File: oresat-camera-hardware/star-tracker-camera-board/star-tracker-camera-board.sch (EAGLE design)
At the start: 46 parts, among them J1 3-1734742-6, U1 AR0134CSSM00SPCA0, U2 TPS70618DRVR, U3 TPS71928-28DRVT, U4 TPS71928-28DRVT, X1 KC2520B27.0000C10E00

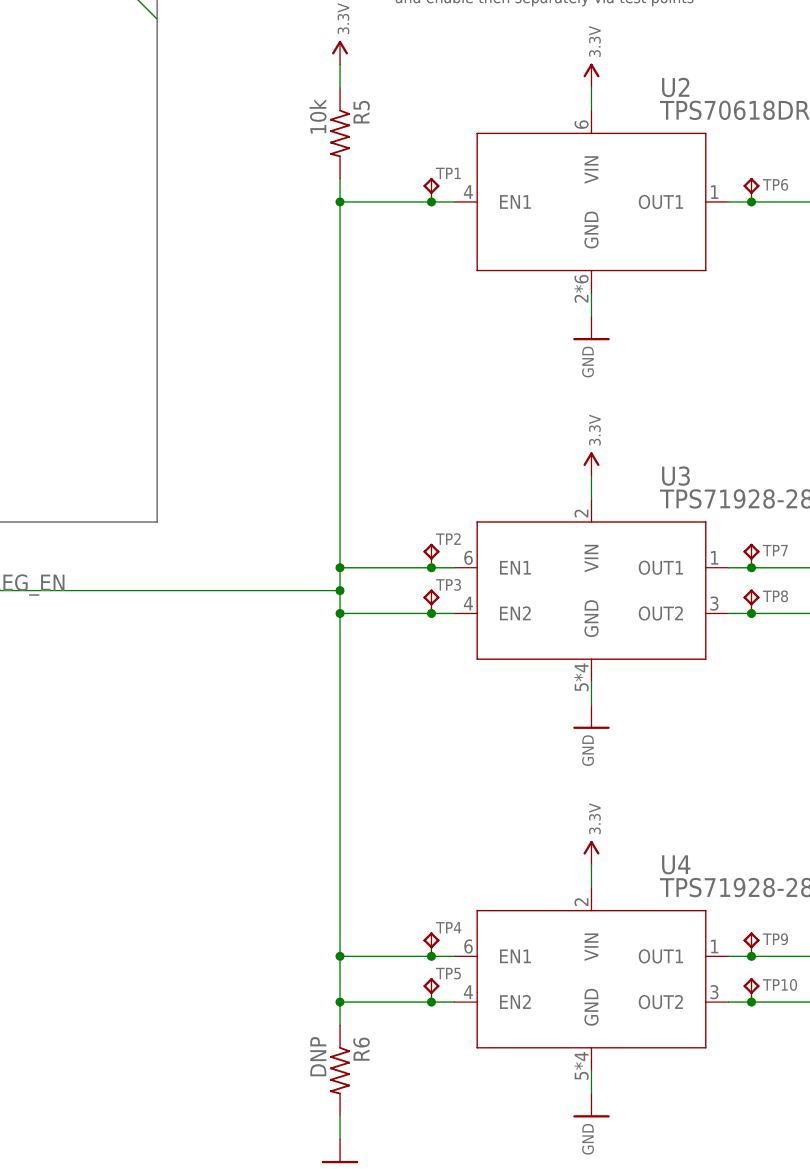
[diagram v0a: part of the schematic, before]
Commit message: updated the star tracker camera board with smaller dimensions
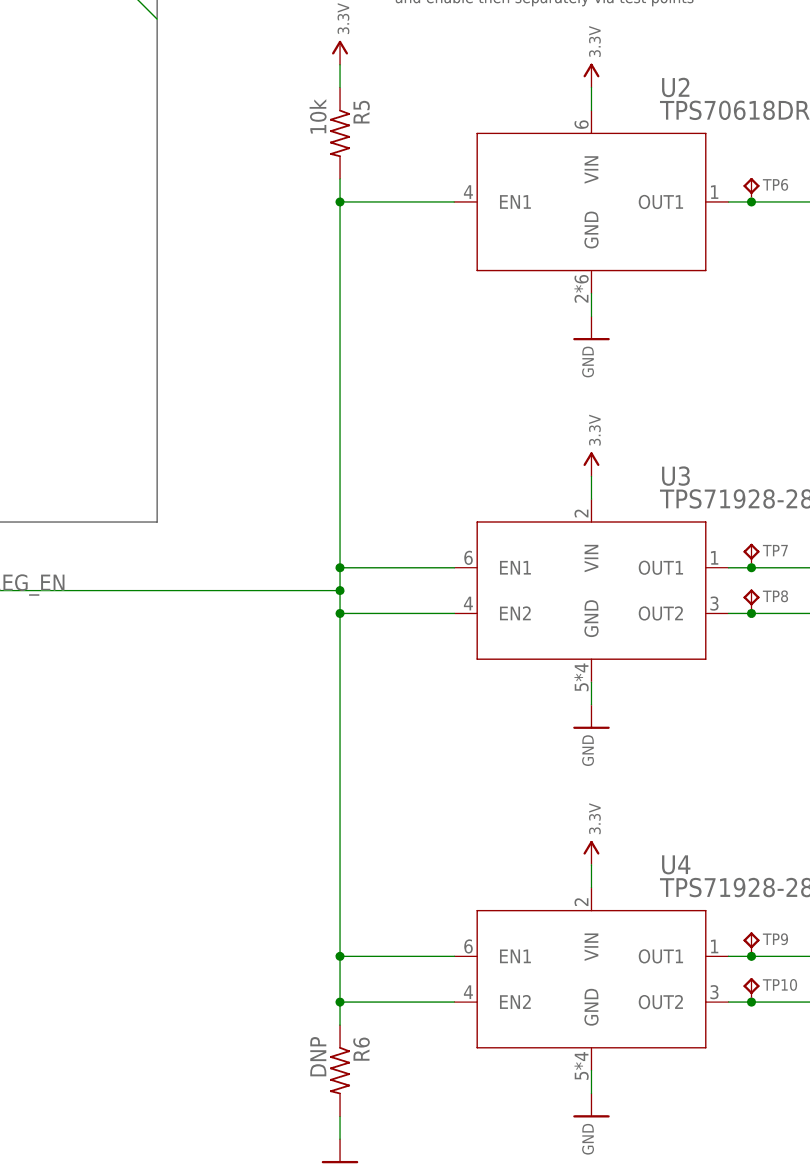
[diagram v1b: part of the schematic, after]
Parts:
- removed TP1, TP2, TP3, TP4, TP5: TPTP06R, J-TestPoint-Small:TPTP06R
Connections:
- net VREG_EN: no longer TP1.TP, TP2.TP, TP3.TP, TP4.TP, TP5.TP
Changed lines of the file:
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@@
 <?xml version="1.0" encoding="utf-8"?>
 <!DOCTYPE eagle SYSTEM "eagle.dtd">
-<eagle version="9.6.1">
+<eagle version="9.6.2">
 <drawing>
 <settings>
@@
 <part name="TP9" library="J-TestPoint-Small" deviceset="TP" device="TP06R" package3d_urn="urn:adsk.eagle:package:27954/1"/>
 <part name="TP10" library="J-TestPoint-Small" deviceset="TP" device="TP06R" package3d_urn="urn:adsk.eagle:package:27954/1"/>
-<part name="TP2" library="J-TestPoint-Small" deviceset="TP" device="TP06R" package3d_urn="urn:adsk.eagle:package:27954/1"/>
-<part name="TP3" library="J-TestPoint-Small" deviceset="TP" device="TP06R" package3d_urn="urn:adsk.eagle:package:27954/1"/>
-<part name="TP4" library="J-TestPoint-Small" deviceset="TP" device="TP06R" package3d_urn="urn:adsk.eagle:package:27954/1"/>
-<part name="TP5" library="J-TestPoint-Small" deviceset="TP" device="TP06R" package3d_urn="urn:adsk.eagle:package:27954/1"/>
 <part name="U2" library="U-TI-TPS70618-VoltageReg" deviceset="TPS70618DRVR" device=""/>
 <part name="SUPPLY10" library="SparkFun-PowerSymbols" deviceset="3.3V" device=""/>
 <part name="GND8" library="SparkFun-PowerSymbols" deviceset="GND" device=""/>
-<part name="TP1" library="J-TestPoint-Small" deviceset="TP" device="TP06R" package3d_urn="urn:adsk.eagle:package:27954/1"/>
 <part name="C19" library="oresat-rcl" deviceset="C-EU" device="0603-C-NOSILK" value="2.2uF"/>
 <part name="TP6" library="J-TestPoint-Small" deviceset="TP" device="TP06R" package3d_urn="urn:adsk.eagle:package:27954/1"/>
@@
 <attribute name="TP_SIGNAL_NAME" x="336.55" y="74.93" size="1.778" layer="97"/>
 </instance>
-<instance part="TP2" gate="G$1" x="299.72" y="124.46" smashed="yes">
-<attribute name="NAME" x="300.228" y="124.46" size="1.27" layer="95"/>
-<attribute name="TP_SIGNAL_NAME" x="300.99" y="123.19" size="1.778" layer="97"/>
-</instance>
-<instance part="TP3" gate="G$1" x="299.72" y="119.38" smashed="yes">
-<attribute name="NAME" x="300.228" y="119.38" size="1.27" layer="95"/>
-<attribute name="TP_SIGNAL_NAME" x="300.99" y="118.11" size="1.778" layer="97"/>
-</instance>
-<instance part="TP4" gate="G$1" x="299.72" y="81.28" smashed="yes">
-<attribute name="NAME" x="300.228" y="81.28" size="1.27" layer="95"/>
-<attribute name="TP_SIGNAL_NAME" x="300.99" y="80.01" size="1.778" layer="97"/>
-</instance>
-<instance part="TP5" gate="G$1" x="299.72" y="76.2" smashed="yes">
-<attribute name="NAME" x="300.228" y="76.2" size="1.27" layer="95"/>
-<attribute name="TP_SIGNAL_NAME" x="300.99" y="74.93" size="1.778" layer="97"/>
-</instance>
 <instance part="U2" gate="A" x="317.5" y="162.56" smashed="yes">
 <attribute name="NAME" x="325.12" y="174.244" size="2.0828" layer="95" ratio="6" rot="SR0"/>
@@
 <instance part="GND8" gate="1" x="317.5" y="147.32" smashed="yes">
 <attribute name="VALUE" x="316.484" y="144.78" size="1.27" layer="96" rot="R90" align="top-center"/>
-</instance>
-<instance part="TP1" gate="G$1" x="299.72" y="165.1" smashed="yes">
-<attribute name="NAME" x="300.228" y="165.1" size="1.27" layer="95"/>
-<attribute name="TP_SIGNAL_NAME" x="300.99" y="163.83" size="1.778" layer="97"/>
 </instance>
 <instance part="C19" gate="CE" x="411.48" y="101.6" smashed="yes">
@@
 <wire x1="289.56" y1="162.56" x2="289.56" y2="121.92" width="0.1524" layer="91"/>
 <wire x1="289.56" y1="121.92" x2="289.56" y2="119.38" width="0.1524" layer="91"/>
-<wire x1="302.26" y1="162.56" x2="299.72" y2="162.56" width="0.1524" layer="91"/>
-<pinref part="TP1" gate="G$1" pin="TP"/>
-<wire x1="299.72" y1="162.56" x2="289.56" y2="162.56" width="0.1524" layer="91"/>
-<junction x="299.72" y="162.56"/>
+<wire x1="302.26" y1="162.56" x2="289.56" y2="162.56" width="0.1524" layer="91"/>
 <junction x="289.56" y="162.56"/>
 <pinref part="U3" gate="A" pin="EN1"/>
-<wire x1="302.26" y1="121.92" x2="299.72" y2="121.92" width="0.1524" layer="91"/>
-<pinref part="TP2" gate="G$1" pin="TP"/>
-<wire x1="299.72" y1="121.92" x2="289.56" y2="121.92" width="0.1524" layer="91"/>
-<junction x="299.72" y="121.92"/>
+<wire x1="302.26" y1="121.92" x2="289.56" y2="121.92" width="0.1524" layer="91"/>
 <junction x="289.56" y="121.92"/>
 <pinref part="U3" gate="A" pin="EN2"/>
-<wire x1="302.26" y1="116.84" x2="299.72" y2="116.84" width="0.1524" layer="91"/>
-<pinref part="TP3" gate="G$1" pin="TP"/>
-<wire x1="299.72" y1="116.84" x2="289.56" y2="116.84" width="0.1524" layer="91"/>
-<junction x="299.72" y="116.84"/>
+<wire x1="302.26" y1="116.84" x2="289.56" y2="116.84" width="0.1524" layer="91"/>
 <junction x="289.56" y="116.84"/>
 <pinref part="U4" gate="A" pin="EN1"/>
-<wire x1="302.26" y1="78.74" x2="299.72" y2="78.74" width="0.1524" layer="91"/>
-<pinref part="TP4" gate="G$1" pin="TP"/>
-<wire x1="299.72" y1="78.74" x2="289.56" y2="78.74" width="0.1524" layer="91"/>
-<junction x="299.72" y="78.74"/>
+<wire x1="302.26" y1="78.74" x2="289.56" y2="78.74" width="0.1524" layer="91"/>
 <junction x="289.56" y="78.74"/>
 <pinref part="U4" gate="A" pin="EN2"/>
-<wire x1="302.26" y1="73.66" x2="299.72" y2="73.66" width="0.1524" layer="91"/>
-<pinref part="TP5" gate="G$1" pin="TP"/>
-<wire x1="299.72" y1="73.66" x2="289.56" y2="73.66" width="0.1524" layer="91"/>
-<junction x="299.72" y="73.66"/>
+<wire x1="302.26" y1="73.66" x2="289.56" y2="73.66" width="0.1524" layer="91"/>
 <junction x="289.56" y="73.66"/>
 <label x="160.02" y="111.76" size="1.778" layer="95" rot="R90"/>
